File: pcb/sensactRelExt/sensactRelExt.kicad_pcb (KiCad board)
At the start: 2 copper layers, 50 x 50 mm, 10 parts, among them P1 CONN_01X02, P2 CONN_02X05, P3 CONN_02X16, U1 DRV8860woPad, U2 DRV8860woPad

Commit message: Unspecified
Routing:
- net Net-(R1-Pad1): track 25.5 -> 24.7 mm
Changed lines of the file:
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@@
-(kicad_pcb (version 4) (host pcbnew 4.0.1-stable)
+(kicad_pcb (version 4) (host pcbnew 4.0.0-stable)
   (general
     (links 61)
     (no_connects 0)
-    (area 99.924999 99.924999 150.075001 150.075001)
+    (area 99.924999 95.529 156.781001 150.075001)
     (thickness 1.6)
     (drawings 4)
@@
   (page A4)
   (layers
-    (0 F.Cu signal)
-    (31 B.Cu signal hide)
+    (0 F.Cu signal hide)
+    (31 B.Cu signal)
     (32 B.Adhes user hide)
     (33 F.Adhes user hide)
     (34 B.Paste user hide)
     (35 F.Paste user hide)
-    (36 B.SilkS user)
-    (37 F.SilkS user)
-    (38 B.Mask user)
-    (39 F.Mask user)
-    (40 Dwgs.User user)
-    (41 Cmts.User user)
-    (42 Eco1.User user)
-    (43 Eco2.User user)
-    (44 Edge.Cuts user)
-    (45 Margin user)
-    (46 B.CrtYd user)
-    (47 F.CrtYd user)
+    (36 B.SilkS user hide)
+    (37 F.SilkS user hide)
+    (38 B.Mask user hide)
+    (39 F.Mask user hide)
+    (40 Dwgs.User user hide)
+    (41 Cmts.User user hide)
+    (42 Eco1.User user hide)
+    (43 Eco2.User user hide)
+    (44 Edge.Cuts user hide)
+    (45 Margin user hide)
+    (46 B.CrtYd user hide)
+    (47 F.CrtYd user hide)
     (48 B.Fab user)
     (49 F.Fab user)
@@
     (pad_to_mask_clearance 0.2)
     (aux_axis_origin 0 0)
-    (visible_elements FFFFFF7F)
+    (visible_elements 7FFFFFFF)
     (pcbplotparams
       (layerselection 0x00030_80000001)
@@
   (segment (start 132.995 128.117) (end 134.366 126.746) (width 0.25) (layer B.Cu) (net 3))
   (segment (start 136.398 118.618) (end 131.318 118.618) (width 0.25) (layer F.Cu) (net 3))
+  (segment (start 132.922 113.792) (end 131.318 115.396) (width 0.25) (layer B.Cu) (net 4))
+  (segment (start 131.318 115.396) (end 131.318 116.078) (width 0.25) (layer B.Cu) (net 4))
   (segment (start 132.432 103.165) (end 134.28 103.165) (width 0.25) (layer B.Cu) (net 4))
   (segment (start 136.398 107.315) (end 136.398 116.078) (width 0.25) (layer B.Cu) (net 4))
   (segment (start 136.398 105.283) (end 136.398 107.315) (width 0.25) (layer B.Cu) (net 4))
   (segment (start 134.28 103.165) (end 136.398 105.283) (width 0.25) (layer B.Cu) (net 4))
-  (segment (start 132.922 113.792) (end 132.922 114.474) (width 0.25) (layer B.Cu) (net 4))
-  (segment (start 132.922 114.474) (end 131.318 116.078) (width 0.25) (layer B.Cu) (net 4))
   (segment (start 131.318 116.078) (end 136.398 116.078) (width 0.25) (layer F.Cu) (net 4))
   (segment (start 128.7145 129.0955) (end 128.7145 135.6995) (width 0.25) (layer B.Cu) (net 5))
@@
   (segment (start 140.000994 129.084586) (end 140.000994 134.795392) (width 0.25) (layer B.Cu) (net 24))
   (segment (start 139.683408 128.767) (end 140.000994 129.084586) (width 0.25) (layer B.Cu) (net 24))
-  (segment (start 132.432 105.765) (end 130.455 105.765) (width 0.25) (layer B.Cu) (net 25) (status 10))
-  (segment (start 129.159 114.601) (end 129.286 114.728) (width 0.25) (layer B.Cu) (net 25))
-  (segment (start 129.159 107.061) (end 129.159 114.601) (width 0.25) (layer B.Cu) (net 25))
-  (segment (start 130.455 105.765) (end 129.159 107.061) (width 0.25) (layer B.Cu) (net 25))
+  (segment (start 132.432 105.765) (end 130.709 105.765) (width 0.25) (layer B.Cu) (net 25))
+  (segment (start 129.286 112.856) (end 130.222 113.792) (width 0.25) (layer B.Cu) (net 25))
+  (segment (start 129.286 107.188) (end 129.286 112.856) (width 0.25) (layer B.Cu) (net 25))
+  (segment (start 130.709 105.765) (end 129.286 107.188) (width 0.25) (layer B.Cu) (net 25))
   (segment (start 131.416 125.517) (end 129.708 125.517) (width 0.25) (layer B.Cu) (net 25))
   (segment (start 129.286 114.728) (end 129.3095 114.7045) (width 0.25) (layer B.Cu) (net 25))

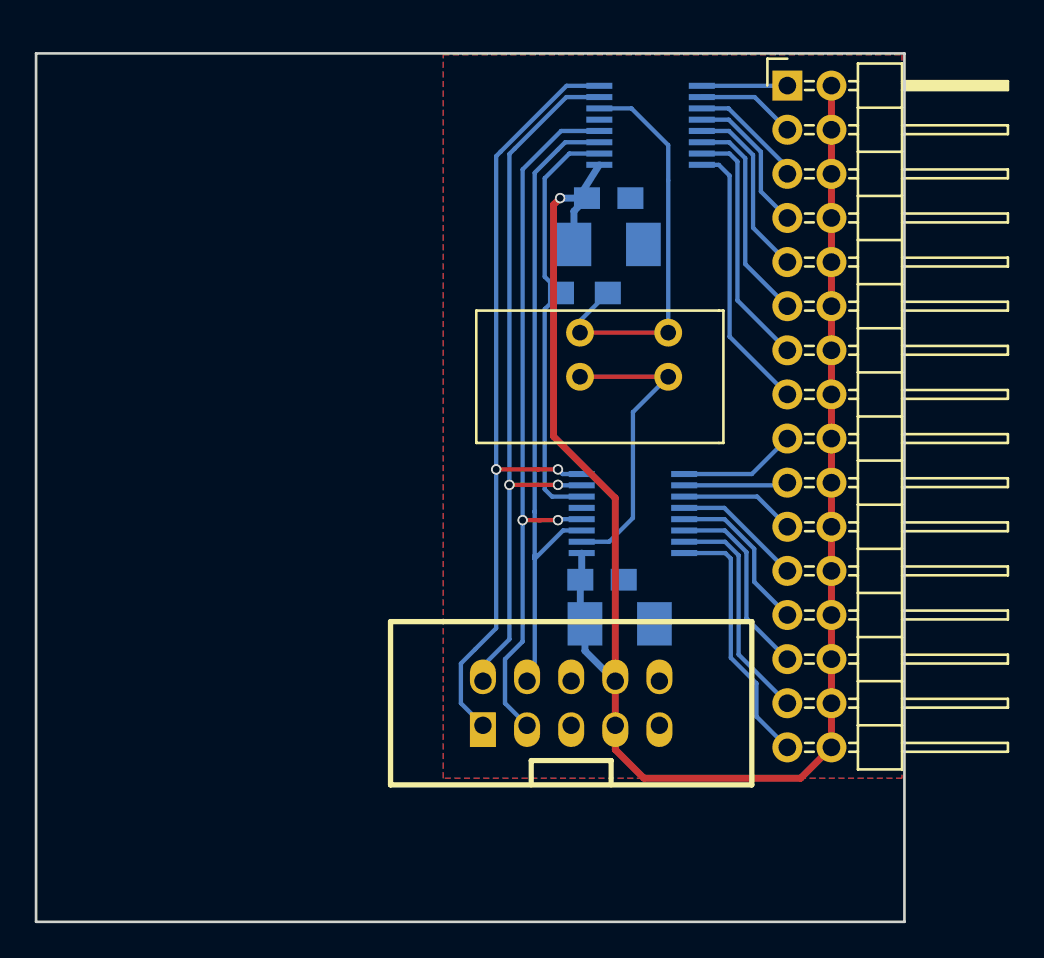
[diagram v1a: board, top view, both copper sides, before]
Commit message: Redesign sensactRelExt
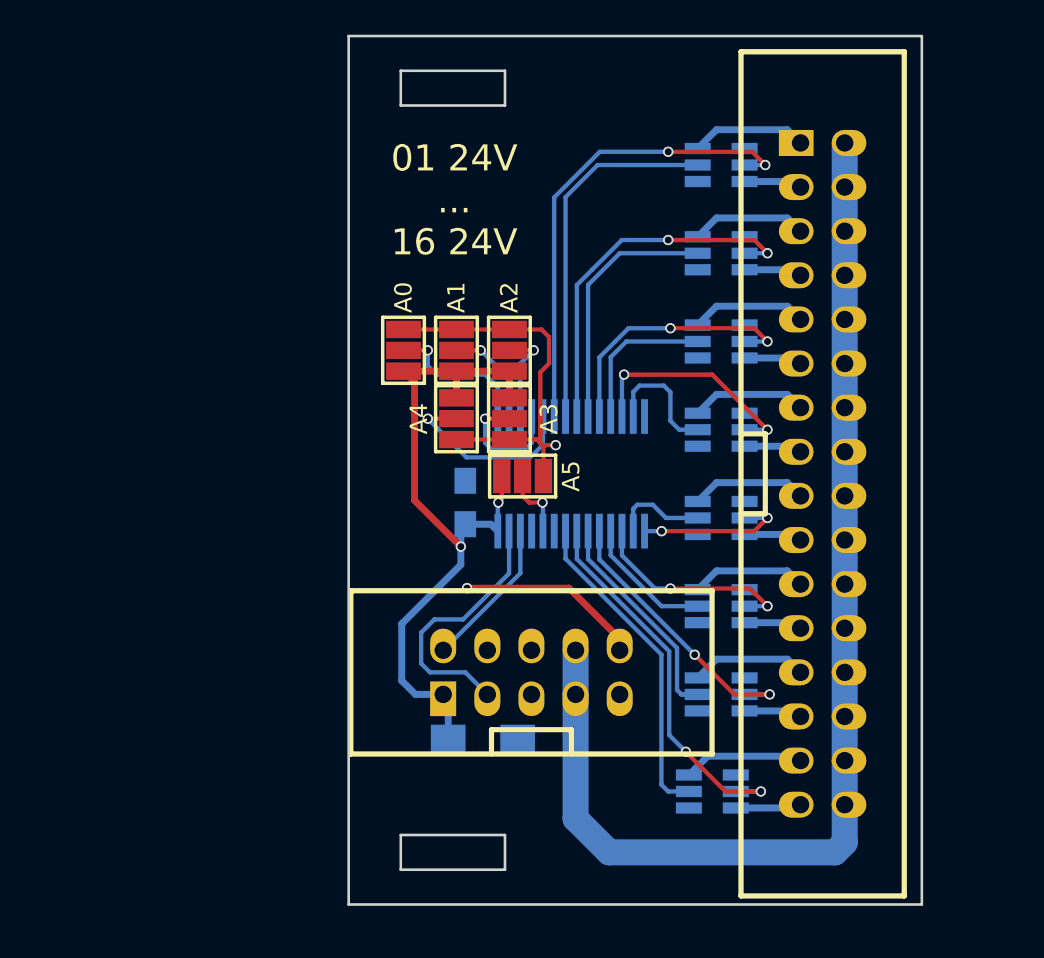
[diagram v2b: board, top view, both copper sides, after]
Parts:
- removed C3: 10u, Capacitors_SMD:C_1210_HandSoldering
- removed C4: u1, Capacitors_SMD:C_0805_HandSoldering
- removed P3: CONN_02X16, Pin_Headers:Pin_Header_Angled_2x16
- removed R1: 0R, Resistors_SMD:R_0805_HandSoldering
- added JP1: A0, sensact:SMD-solder-bridge-3pin, F.Cu at (121.2, 117.1)
- added JP2: A1, sensact:SMD-solder-bridge-3pin, F.Cu at (124.2, 117.1)
- added JP3: A2, sensact:SMD-solder-bridge-3pin, F.Cu at (127.3, 117.1)
- added JP4: A3, sensact:SMD-solder-bridge-3pin, F.Cu at (127.3, 121.0)
- added JP5: A4, sensact:SMD-solder-bridge-3pin, F.Cu at (124.2, 121.0)
- added JP6: A5, sensact:SMD-solder-bridge-3pin, F.Cu at (128.0, 124.3)
- added U3: NUD3124DMT1G, sensact:SOT-23-6_handsolder, B.Cu at (139.4, 116.6)
- added U4: NUD3124DMT1G, sensact:SOT-23-6_handsolder, B.Cu at (139.4, 121.7)
- added U5: NUD3124DMT1G, sensact:SOT-23-6_handsolder, B.Cu at (139.4, 126.7)
- added U6: NUD3124DMT1G, sensact:SOT-23-6_handsolder, B.Cu at (139.4, 131.8)
- added U7: NUD3124DMT1G, sensact:SOT-23-6_handsolder, B.Cu at (139.4, 136.9)
- added U8: NUD3124DMT1G, sensact:SOT-23-6_handsolder, B.Cu at (138.9, 142.5)
- added U9: PCA9685, sensact:TSSOP-28_4.4x9.7mm_Pitch0.65mm_handsolder, B.Cu at (130.8, 124.2)
- C1: value 10u -> u1; footprint Capacitors_SMD:C_1210_HandSoldering -> Capacitors_SMD:C_0805_HandSoldering
- C2: value u1 -> 10u; footprint Capacitors_SMD:C_0805_HandSoldering -> Capacitors_SMD:C_1206_HandSoldering
- P1: value CONN_01X02 -> CONN_02X05; footprint sensact:KF141R-2p -> w_conn_strip:vasch_strip_5x2
- P2: value CONN_02X05 -> CONN_02X16; footprint w_conn_strip:vasch_strip_5x2 -> w_conn_strip:vasch_strip_16x2
- U1, U2: value DRV8860woPad -> NUD3124DMT1G; footprint sensact:TSSOP-16_4.4x5mm_Pitch0.65mm_narrowPad -> sensact:SOT-23-6_handsolder
- moved C2 31.9 mm to (125.7, 139.4)
- moved U1 20.7 mm to (139.4, 106.4), turned to 180 degrees
- moved P2 19.6 mm to (145.3, 124.2), turned to 270 degrees
- moved P1 17.8 mm to (128.5, 135.6), turned to 0 degrees
- moved C1 11.3 mm to (124.7, 125.9), turned to 90 degrees
- moved U2 8.41 mm to (139.4, 111.5), turned to 180 degrees
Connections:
- C1 pad 1: +24V -> +3V3
- C2 pad 1: +24V -> +3V3
- P1 pad 1: /DOUT -> +3V3
- P1 pad 2: /DIN -> /SCL
- P2 pad 1: /ENABLE -> Net-(P2-Pad1)
- P2 pad 10: GND -> +24V
- P2 pad 2: /FAULT -> +24V
- P2 pad 3: /LAT -> Net-(P2-Pad3)
- P2 pad 4: /CLK -> +24V
- P2 pad 5: (no net) -> Net-(P2-Pad5)
- P2 pad 6: (no net) -> +24V
- P2 pad 7: +24V -> Net-(P2-Pad7)
- P2 pad 9: GND -> Net-(P2-Pad9)
- U1 pad 1: +24V -> GND
- U1 pad 2: /DIN -> /LED0
- U1 pad 3: /CLK -> Net-(P2-Pad3)
- U1 pad 4: /LAT -> GND
- U1 pad 5: GND -> /LED1
- U1 pad 6: Net-(R1-Pad1) -> Net-(P2-Pad1)
- U2 pad 1: +24V -> GND
- U2 pad 2: Net-(R1-Pad1) -> /LED2
- U2 pad 3: /CLK -> Net-(P2-Pad7)
- U2 pad 4: /LAT -> GND
- U2 pad 5: GND -> /LED3
- U2 pad 6: /DOUT -> Net-(P2-Pad5)
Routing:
- net /ENABLE: track 46.8 -> 0.00 mm, vias 2 -> 0
- net +3V3: track 0.00 -> 41.9 mm, vias 0 -> 2
- net /LAT: track 41.8 -> 0.00 mm, vias 2 -> 0
- net /FAULT: track 41.7 -> 0.00 mm, vias 2 -> 0
- net /CLK: track 37.6 -> 0.00 mm
- net GND: track 0.00 -> 34.5 mm, vias 0 -> 2
- net +24V: track 100.4 -> 66.5 mm, vias 1 -> 0
- net /LED0: track 0.00 -> 27.4 mm, vias 0 -> 2
- net Net-(R1-Pad1): track 24.7 -> 0.00 mm
- net /DOUT: track 23.7 -> 0.00 mm
- net /LED14: track 0.00 -> 22.0 mm, vias 0 -> 2
- net /LED2: track 0.00 -> 21.3 mm, vias 0 -> 2
- net /LED1: track 0.00 -> 21.0 mm
- net /LED15: track 0.00 -> 18.6 mm
- net /DIN: track 17.6 -> 0.00 mm
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- added copper zone on F.Cu, net GND
- removed copper zone on F.Cu, net +24V
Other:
- board size 50 x 50 mm -> 33 x 50 mm
- net class HIGH_POWER added: clearance 0.3, trace_width 1, via_dia 1.27, via_drill 0.8
- board text added: "01 24V ... 16 24V"

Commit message: Finalize Extension Modules PCB order
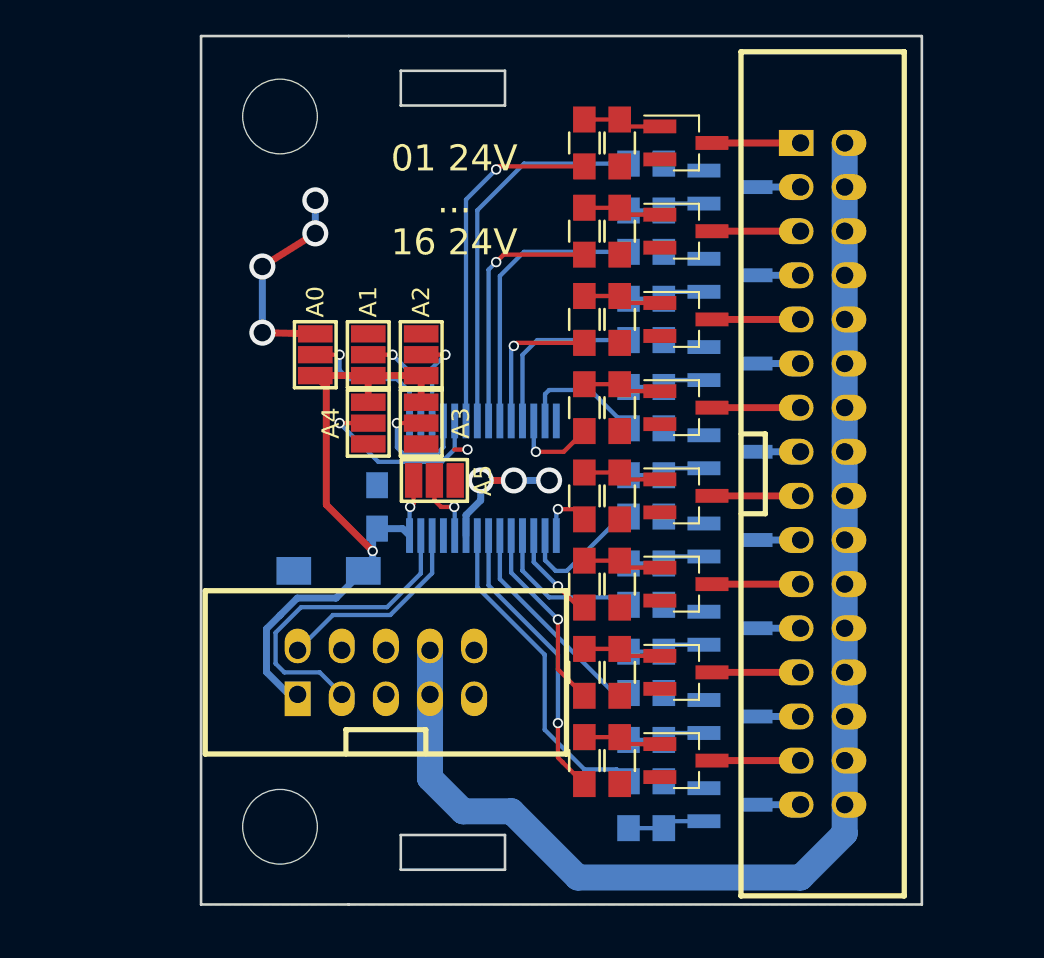
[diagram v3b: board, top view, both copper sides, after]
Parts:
- removed U1, U2, U3, U4, U5, U6, U7, U8: NUD3124DMT1G, sensact:SOT-23-6_handsolder
- added M1: CONN_01X01, Mounting_Holes:MountingHole_4.3mm_M4_DIN965, F.Cu at (114.0, 144.5)
- added M2: CONN_01X01, Mounting_Holes:MountingHole_4.3mm_M4_DIN965, F.Cu at (114.0, 103.6)
- added Q1: Q_NMOS_GSD, TO_SOT_Packages_SMD:SOT-23_Handsoldering, F.Cu at (137.4, 105.2)
- added Q10: Q_NMOS_GSD, TO_SOT_Packages_SMD:SOT-23_Handsoldering, B.Cu at (140.0, 128.0)
- added Q11: Q_NMOS_GSD, TO_SOT_Packages_SMD:SOT-23_Handsoldering, F.Cu at (137.4, 130.6)
- added Q12: Q_NMOS_GSD, TO_SOT_Packages_SMD:SOT-23_Handsoldering, B.Cu at (140.0, 133.1)
- added Q13: Q_NMOS_GSD, TO_SOT_Packages_SMD:SOT-23_Handsoldering, F.Cu at (137.4, 135.6)
- added Q14: Q_NMOS_GSD, TO_SOT_Packages_SMD:SOT-23_Handsoldering, B.Cu at (140.0, 138.2)
- added Q15: Q_NMOS_GSD, TO_SOT_Packages_SMD:SOT-23_Handsoldering, F.Cu at (137.4, 140.7)
- added Q16: Q_NMOS_GSD, TO_SOT_Packages_SMD:SOT-23_Handsoldering, B.Cu at (140.0, 143.3)
- added Q2: Q_NMOS_GSD, TO_SOT_Packages_SMD:SOT-23_Handsoldering, B.Cu at (140.0, 107.7)
- added Q3: Q_NMOS_GSD, TO_SOT_Packages_SMD:SOT-23_Handsoldering, F.Cu at (137.4, 110.2)
- added Q4: Q_NMOS_GSD, TO_SOT_Packages_SMD:SOT-23_Handsoldering, B.Cu at (140.0, 112.8)
- added Q5: Q_NMOS_GSD, TO_SOT_Packages_SMD:SOT-23_Handsoldering, F.Cu at (137.4, 115.3)
- added Q6: Q_NMOS_GSD, TO_SOT_Packages_SMD:SOT-23_Handsoldering, B.Cu at (140.0, 117.9)
- added Q7: Q_NMOS_GSD, TO_SOT_Packages_SMD:SOT-23_Handsoldering, F.Cu at (137.4, 120.4)
- added Q8: Q_NMOS_GSD, TO_SOT_Packages_SMD:SOT-23_Handsoldering, B.Cu at (140.0, 122.9)
- added Q9: Q_NMOS_GSD, TO_SOT_Packages_SMD:SOT-23_Handsoldering, F.Cu at (137.4, 125.5)
- added R1: 1k, Resistors_SMD:R_0805_HandSoldering, F.Cu at (131.6, 105.2)
- added R10: 1k, Resistors_SMD:R_0805_HandSoldering, B.Cu at (134.1, 117.9)
- added R11: 10k, Resistors_SMD:R_0805_HandSoldering, F.Cu at (133.6, 115.3)
- added R12: 10k, Resistors_SMD:R_0805_HandSoldering, B.Cu at (136.1, 117.9)
- added R13: 1k, Resistors_SMD:R_0805_HandSoldering, F.Cu at (131.6, 120.4)
- added R14: 1k, Resistors_SMD:R_0805_HandSoldering, B.Cu at (134.1, 122.9)
- added R15: 10k, Resistors_SMD:R_0805_HandSoldering, F.Cu at (133.6, 120.4)
- added R16: 10k, Resistors_SMD:R_0805_HandSoldering, B.Cu at (136.1, 122.9)
- added R17: 1k, Resistors_SMD:R_0805_HandSoldering, F.Cu at (131.6, 125.5)
- added R18: 1k, Resistors_SMD:R_0805_HandSoldering, B.Cu at (134.1, 128.0)
- added R19: 10k, Resistors_SMD:R_0805_HandSoldering, F.Cu at (133.6, 125.5)
- added R2: 1k, Resistors_SMD:R_0805_HandSoldering, B.Cu at (134.1, 107.7)
- added R20: 10k, Resistors_SMD:R_0805_HandSoldering, B.Cu at (136.1, 128.0)
- added R21: 1k, Resistors_SMD:R_0805_HandSoldering, F.Cu at (131.6, 130.6)
- added R22: 1k, Resistors_SMD:R_0805_HandSoldering, B.Cu at (134.1, 133.1)
- added R23: 10k, Resistors_SMD:R_0805_HandSoldering, F.Cu at (133.6, 130.6)
- added R24: 10k, Resistors_SMD:R_0805_HandSoldering, B.Cu at (136.1, 133.1)
- added R25: 1k, Resistors_SMD:R_0805_HandSoldering, F.Cu at (131.6, 135.6)
- added R26: 1k, Resistors_SMD:R_0805_HandSoldering, B.Cu at (134.1, 138.2)
- added R27: 10k, Resistors_SMD:R_0805_HandSoldering, F.Cu at (133.6, 135.6)
- added R28: 10k, Resistors_SMD:R_0805_HandSoldering, B.Cu at (136.1, 138.2)
- added R29: 1k, Resistors_SMD:R_0805_HandSoldering, F.Cu at (131.6, 140.7)
- added R3: 10k, Resistors_SMD:R_0805_HandSoldering, F.Cu at (133.6, 105.2)
- added R30: 10k, Resistors_SMD:R_0805_HandSoldering, F.Cu at (133.6, 140.7)
- added R31: 1k, Resistors_SMD:R_0805_HandSoldering, B.Cu at (134.1, 143.3)
- added R32: 10k, Resistors_SMD:R_0805_HandSoldering, B.Cu at (136.1, 143.3)
- added R4: 10k, Resistors_SMD:R_0805_HandSoldering, B.Cu at (136.1, 107.7)
- added R5: 1k, Resistors_SMD:R_0805_HandSoldering, F.Cu at (131.6, 110.2)
- added R6: 1k, Resistors_SMD:R_0805_HandSoldering, B.Cu at (134.1, 112.8)
- added R7: 10k, Resistors_SMD:R_0805_HandSoldering, F.Cu at (133.6, 110.2)
- added R8: 10k, Resistors_SMD:R_0805_HandSoldering, B.Cu at (136.1, 112.8)
- added R9: 1k, Resistors_SMD:R_0805_HandSoldering, F.Cu at (131.6, 115.3)
- moved C2 13.1 mm to (116.8, 129.8), turned to 180 degrees
- moved P1 8.38 mm to (120.1, 135.6)
- moved C1 5.09 mm to (119.6, 126.1)
- moved JP1 5.09 mm to (116.1, 117.3)
- moved JP2 5.09 mm to (119.1, 117.3)
- moved JP3 5.09 mm to (122.2, 117.3)
- moved JP4 5.09 mm to (122.2, 121.3)
- moved JP5 5.09 mm to (119.1, 121.3)
- moved U9 5.09 mm to (125.7, 124.5)
- moved JP6 5.09 mm to (122.9, 124.6)
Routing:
- net GND: track 34.5 -> 19.8 mm, vias 2 -> 7
- net +24V: track 66.5 -> 75.2 mm
- net /LED6: track 13.4 -> 5.11 mm, vias 2 -> 1
- net /LED0: track 27.4 -> 20.4 mm, vias 2 -> 1
- net /LED4: track 15.4 -> 8.52 mm, vias 2 -> 1
- net /LED10: track 12.3 -> 5.53 mm, vias 2 -> 1
- net /LED2: track 21.3 -> 14.6 mm, vias 2 -> 1
- net /LED14: track 22.0 -> 16.6 mm, vias 2 -> 1
- net /LED8: track 8.71 -> 3.33 mm, vias 2 -> 1
- net /LED12: track 16.1 -> 11.0 mm, vias 2 -> 1
- net Net-(Q8-Pad1): track 0.00 -> 4.51 mm
- net Net-(Q6-Pad1): track 0.00 -> 4.51 mm
- net Net-(Q4-Pad1): track 0.00 -> 4.51 mm
- net Net-(Q2-Pad1): track 0.00 -> 4.51 mm
- net Net-(Q16-Pad1): track 0.00 -> 4.51 mm
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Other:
- board size 33 x 50 mm -> 41.5 x 50 mm
